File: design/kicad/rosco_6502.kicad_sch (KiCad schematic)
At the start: 54 parts, among them IC1 W65C02SxP, IC2 ATF22V10C-7PX, IC3 XR68C681CJTR-F, IC4 NE555P, IC5 ATF22V10C-7PX, J1 UART_A, J2 UART_B, J3 Conn_01x06, J4 Conn_01x01_Male, J5 Conn_02x18_Odd_Even, J6 Conn_01x02_Male, Q1 3.6864MHz, U1 AS6C4008-55PCN, U2 AS6C62256-55PCN, U3 AT28C64B-15PU, U4 74HCT174, X1 14MHz

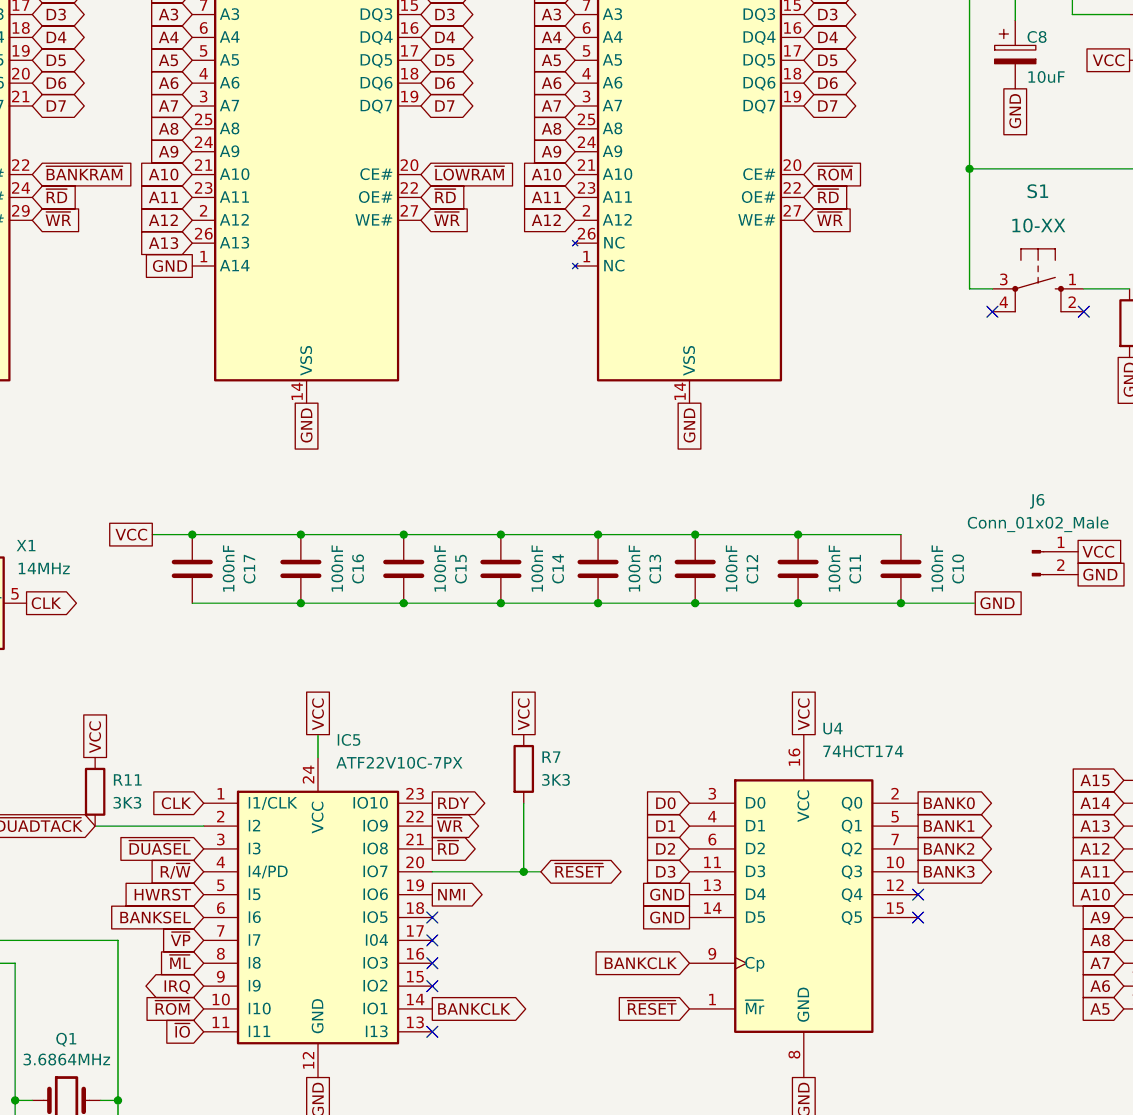
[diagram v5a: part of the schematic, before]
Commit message: Speedier ROM fixes
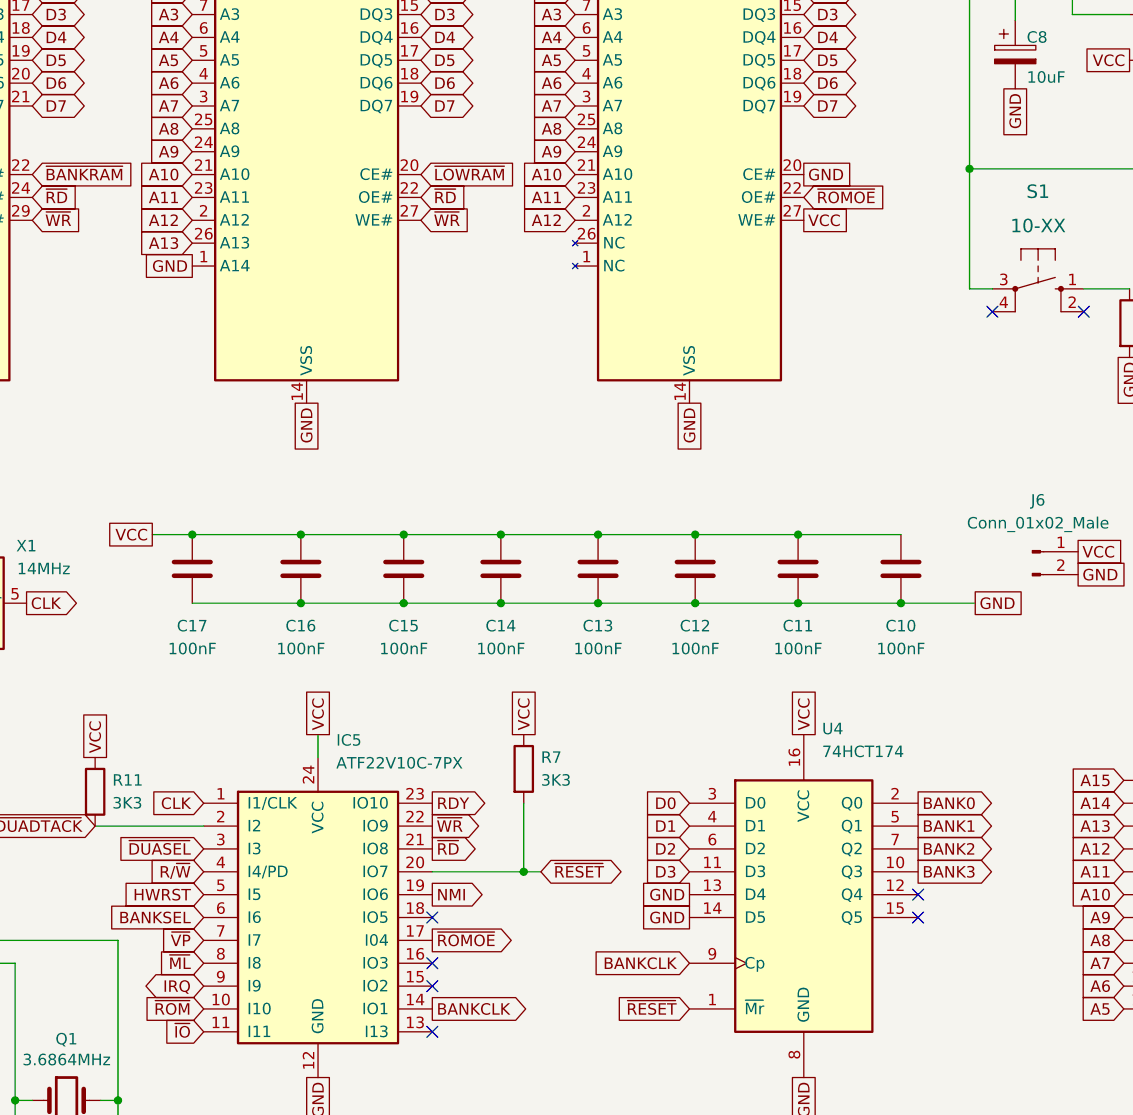
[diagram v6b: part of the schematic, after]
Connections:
- net GND: now also U3.20 (CE#)
- net VCC: now also U3.27 (WE#)
- net ~{RD}: no longer U3.22 (OE#)
- net ~{ROM}: no longer U3.20 (CE#)
- net ~{WR}: no longer U3.27 (WE#)
- net ~{ROMOE}: now reaches IC5.17 (I04)
- net ~{ROMOE}: now also U3.22 (OE#)
- no-connect marks 15 -> 14
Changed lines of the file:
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@@
   (no_connect (at 166.37 140.335))
   (no_connect (at 166.37 135.255))
-  (no_connect (at 166.37 137.795))
   (no_connect (at 106.68 127.635))
   (no_connect (at 50.8 37.465))
@@
     )
   )
-  (global_label "~{ROM}" (shape input) (at 207.645 52.705 0) (fields_autoplaced)
-    (effects (font (size 1.27 1.27)) (justify left))
-    (property "Intersheet References" "${INTERSHEET_REFS}" (id 0) (at 214.11 52.6256 0)
-      (effects (font (size 1.27 1.27)) (justify left) hide)
-    )
-  )
   (global_label "VCC" (shape passive) (at 176.53 114.935 90) (fields_autoplaced)
     (effects (font (size 1.27 1.27)) (justify left))
@@
     )
   )
+  (global_label "VCC" (shape passive) (at 207.645 57.785 0) (fields_autoplaced)
+    (effects (font (size 1.27 1.27)) (justify left))
+    (property "Intersheet References" "${INTERSHEET_REFS}" (id 0) (at 213.6867 57.7056 0)
+      (effects (font (size 1.27 1.27)) (justify left) hide)
+    )
+  )
   (global_label "A1" (shape input) (at 72.39 127.635 180) (fields_autoplaced)
     (effects (font (size 1.27 1.27)) (justify right))
@@
     )
   )
-  (global_label "~{RD}" (shape input) (at 207.645 55.245 0) (fields_autoplaced)
+  (global_label "~{ROMOE}" (shape input) (at 207.645 55.245 0) (fields_autoplaced)
     (effects (font (size 1.27 1.27)) (justify left))
-    (property "Intersheet References" "${INTERSHEET_REFS}" (id 0) (at 212.5981 55.1656 0)
+    (property "Intersheet References" "${INTERSHEET_REFS}" (id 0) (at 216.5895 55.1656 0)
       (effects (font (size 1.27 1.27)) (justify left) hide)
     )
@@
     )
   )
+  (global_label "~{ROMOE}" (shape output) (at 166.37 137.795 0) (fields_autoplaced)
+    (effects (font (size 1.27 1.27)) (justify left))
+    (property "Intersheet References" "${INTERSHEET_REFS}" (id 0) (at 175.3145 137.7156 0)
+      (effects (font (size 1.27 1.27)) (justify left) hide)
+    )
+  )
   (global_label "VCC" (shape passive) (at 20.32 37.465 90) (fields_autoplaced)
     (effects (font (size 1.27 1.27)) (justify left))
@@
     )
   )
+  (global_label "GND" (shape passive) (at 207.645 52.705 0) (fields_autoplaced)
+    (effects (font (size 1.27 1.27)) (justify left))
+    (property "Intersheet References" "${INTERSHEET_REFS}" (id 0) (at 213.9286 52.7844 0)
+      (effects (font (size 1.27 1.27)) (justify left) hide)
+    )
+  )
   (global_label "~{DUADTACK}" (shape tri_state) (at 128.905 125.095 180) (fields_autoplaced)
     (effects (font (size 1.27 1.27)) (justify right))
@@
     )
   )
-  (global_label "~{WR}" (shape input) (at 207.645 57.785 0) (fields_autoplaced)
-    (effects (font (size 1.27 1.27)) (justify left))
-    (property "Intersheet References" "${INTERSHEET_REFS}" (id 0) (at 212.7795 57.7056 0)
-      (effects (font (size 1.27 1.27)) (justify left) hide)
-    )
-  )
   (global_label "GND" (shape passive) (at 255.905 150.495 270) (fields_autoplaced)
     (effects (font (size 1.27 1.27)) (justify right))
@@
   (symbol (lib_id "Device:C") (at 163.195 96.52 180) (unit 1)
     (in_bom yes) (on_board yes)
-    (property "Reference" "C15" (id 0) (at 169.5958 96.52 90))
-    (property "Value" "100nF" (id 1) (at 167.2844 96.52 90))
+    (property "Reference" "C15" (id 0) (at 163.195 102.87 0))
+    (property "Value" "100nF" (id 1) (at 163.195 105.41 0))
     (property "Footprint" "Capacitor_THT:C_Rect_L4.0mm_W2.5mm_P2.50mm" (id 2) (at 162.2298 92.71 0)
       (effects (font (size 1.27 1.27)) hide)
@@
   (symbol (lib_id "Device:C") (at 173.99 96.52 180) (unit 1)
     (in_bom yes) (on_board yes)
-    (property "Reference" "C14" (id 0) (at 180.3908 96.52 90))
-    (property "Value" "100nF" (id 1) (at 178.0794 96.52 90))
+    (property "Reference" "C14" (id 0) (at 173.99 102.87 0))
+    (property "Value" "100nF" (id 1) (at 173.99 105.41 0))
     (property "Footprint" "Capacitor_THT:C_Rect_L4.0mm_W2.5mm_P2.50mm" (id 2) (at 173.0248 92.71 0)
       (effects (font (size 1.27 1.27)) hide)
@@
   (symbol (lib_id "Device:C") (at 218.44 96.52 180) (unit 1)
     (in_bom yes) (on_board yes)
-    (property "Reference" "C10" (id 0) (at 224.8408 96.52 90))
-    (property "Value" "100nF" (id 1) (at 222.5294 96.52 90))
+    (property "Reference" "C10" (id 0) (at 218.44 102.87 0))
+    (property "Value" "100nF" (id 1) (at 218.44 105.41 0))
     (property "Footprint" "Capacitor_THT:C_Rect_L4.0mm_W2.5mm_P2.50mm" (id 2) (at 217.4748 92.71 0)
       (effects (font (size 1.27 1.27)) hide)
@@
   (symbol (lib_id "Device:C") (at 139.7 96.52 180) (unit 1)
     (in_bom yes) (on_board yes)
-    (property "Reference" "C17" (id 0) (at 146.1008 96.52 90))
-    (property "Value" "100nF" (id 1) (at 143.7894 96.52 90))
+    (property "Reference" "C17" (id 0) (at 139.7 102.87 0))
+    (property "Value" "100nF" (id 1) (at 139.7 105.41 0))
     (property "Footprint" "Capacitor_THT:C_Rect_L4.0mm_W2.5mm_P2.50mm" (id 2) (at 138.7348 92.71 0)
       (effects (font (size 1.27 1.27)) hide)
@@
   (symbol (lib_id "Device:C") (at 184.785 96.52 180) (unit 1)
     (in_bom yes) (on_board yes)
-    (property "Reference" "C13" (id 0) (at 191.1858 96.52 90))
-    (property "Value" "100nF" (id 1) (at 188.8744 96.52 90))
+    (property "Reference" "C13" (id 0) (at 184.785 102.87 0))
+    (property "Value" "100nF" (id 1) (at 184.785 105.41 0))
     (property "Footprint" "Capacitor_THT:C_Rect_L4.0mm_W2.5mm_P2.50mm" (id 2) (at 183.8198 92.71 0)
       (effects (font (size 1.27 1.27)) hide)
@@
   (symbol (lib_id "Device:C") (at 195.58 96.52 180) (unit 1)
     (in_bom yes) (on_board yes)
-    (property "Reference" "C12" (id 0) (at 201.9808 96.52 90))
-    (property "Value" "100nF" (id 1) (at 199.6694 96.52 90))
+    (property "Reference" "C12" (id 0) (at 195.58 102.87 0))
+    (property "Value" "100nF" (id 1) (at 195.58 105.41 0))
     (property "Footprint" "Capacitor_THT:C_Rect_L4.0mm_W2.5mm_P2.50mm" (id 2) (at 194.6148 92.71 0)
       (effects (font (size 1.27 1.27)) hide)
@@
   (symbol (lib_id "Device:C") (at 207.01 96.52 180) (unit 1)
     (in_bom yes) (on_board yes)
-    (property "Reference" "C11" (id 0) (at 213.4108 96.52 90))
-    (property "Value" "100nF" (id 1) (at 211.0994 96.52 90))
+    (property "Reference" "C11" (id 0) (at 207.01 102.87 0))
+    (property "Value" "100nF" (id 1) (at 207.01 105.41 0))
     (property "Footprint" "Capacitor_THT:C_Rect_L4.0mm_W2.5mm_P2.50mm" (id 2) (at 206.0448 92.71 0)
       (effects (font (size 1.27 1.27)) hide)
@@
   (symbol (lib_id "Device:C") (at 151.765 96.52 180) (unit 1)
     (in_bom yes) (on_board yes)
-    (property "Reference" "C16" (id 0) (at 158.1658 96.52 90))
-    (property "Value" "100nF" (id 1) (at 155.8544 96.52 90))
+    (property "Reference" "C16" (id 0) (at 151.765 102.87 0))
+    (property "Value" "100nF" (id 1) (at 151.765 105.41 0))
     (property "Footprint" "Capacitor_THT:C_Rect_L4.0mm_W2.5mm_P2.50mm" (id 2) (at 150.7998 92.71 0)
       (effects (font (size 1.27 1.27)) hide)
